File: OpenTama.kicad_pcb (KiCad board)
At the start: 2 copper layers, 45 x 58.2 mm, 65 parts, among them J1 Conn_01x09, J2 Conn_01x14, J3 Conn_01x07, J4 USB_C_Receptacle_USB2.0, J5 Conn_01x14, Q1 BSS138, Q2 BSS138, Q3 BSS84, SW1 LEFT, SW2 MIDDLE, SW3 RIGHT, U1 TPS62203DBV, U2 LTC4054ES5-4.2, U3 STM32L072CBTx, U4 USBLC6-2SC6, Y1 32768Hz - 12,5 pF

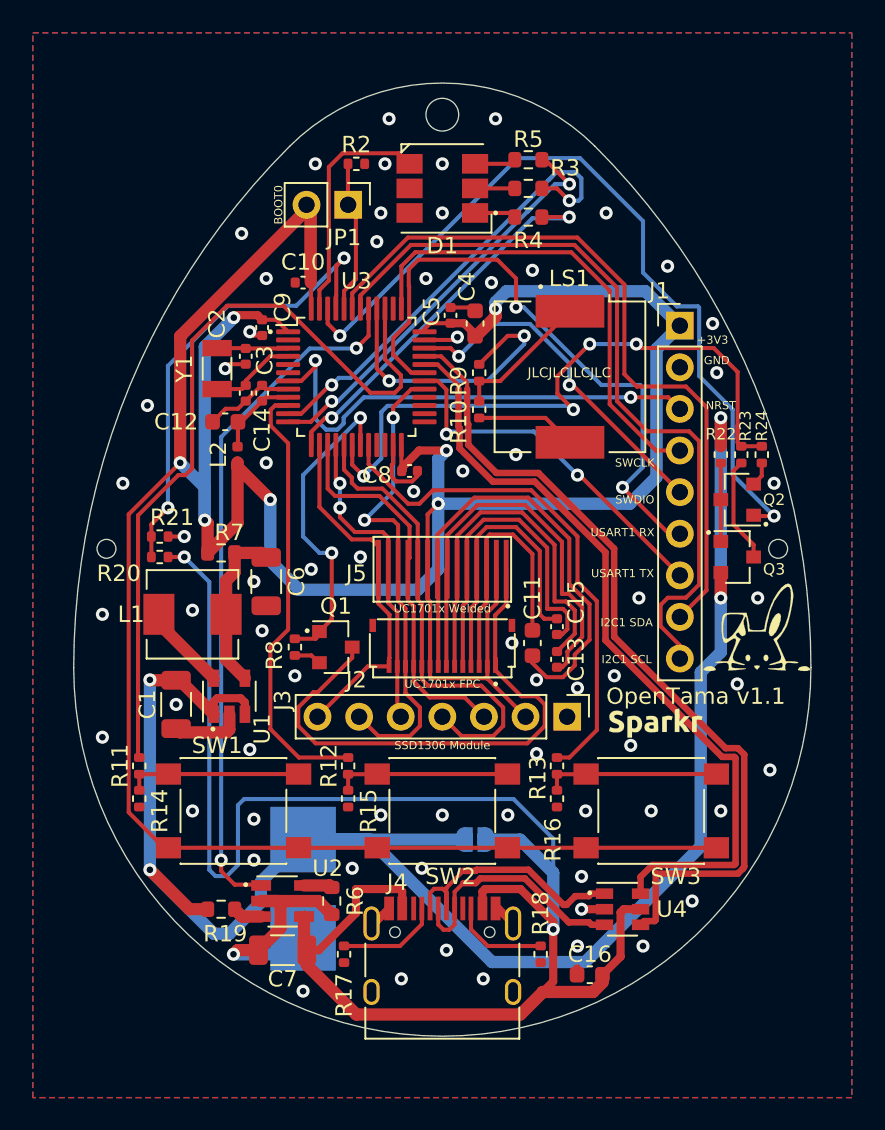
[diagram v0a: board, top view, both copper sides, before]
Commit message: Redesign with ESP32
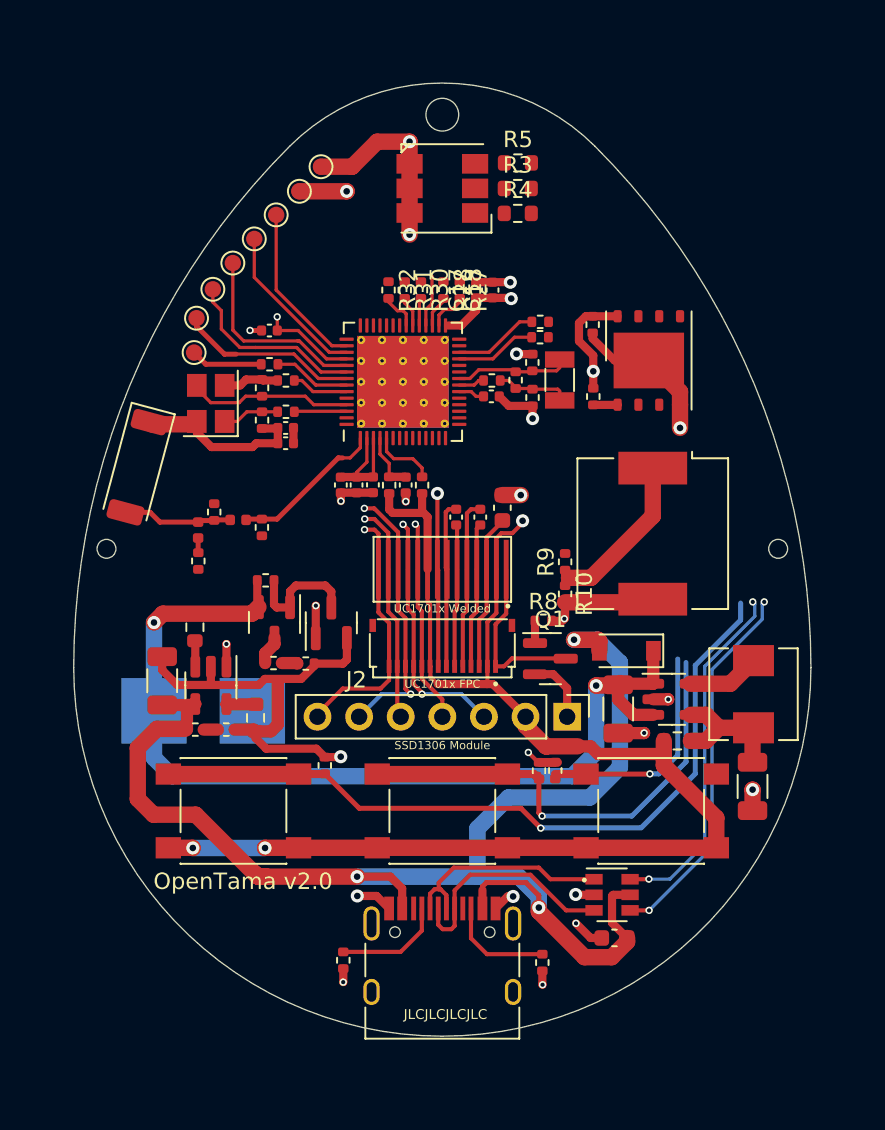
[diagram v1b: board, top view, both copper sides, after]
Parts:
- removed the G*** at (163.0, 104.5)
- removed J1: Conn_01x09, Connector_PinHeader_2.54mm:PinHeader_1x09_P2.54mm_Vertical
- removed JP1: BOOT0, Connector_PinHeader_2.54mm:PinHeader_1x02_P2.54mm_Vertical
- removed JP2: No BATT, Jumper:SolderJumper-2_P1.3mm_Open_RoundedPad1.0x1.5mm
- added AE1: Antenna_Chip, RF_Antenna:Johanson_2450AT43F0100, F.Cu at (131.4, 89.0)
- added C17: 1uF, Capacitor_SMD:C_0402_1005Metric, F.Cu at (152.1, 78.2)
- added C18: 0.1uF, Capacitor_SMD:C_0402_1005Metric, F.Cu at (153.1, 78.2)
- added C19: 10uF, Capacitor_SMD:C_0402_1005Metric, F.Cu at (143.8, 90.1)
- added C20: 0.1uF, Capacitor_SMD:C_0402_1005Metric, F.Cu at (139.4, 80.7)
- added C21: 1uF, Capacitor_SMD:C_0402_1005Metric, F.Cu at (140.4, 87.6)
- added C22: 1uF, Capacitor_SMD:C_0402_1005Metric, F.Cu at (144.8, 90.1)
- added C23: 0.1uF, Capacitor_SMD:C_0402_1005Metric, F.Cu at (140.4, 86.6)
- added C24: 0.1uF, Capacitor_SMD:C_0402_1005Metric, F.Cu at (145.8, 90.1)
- added C25: 0.1uF, Capacitor_SMD:C_0402_1005Metric, F.Cu at (153.0, 84.7)
- added D2: D_Small, Diode_SMD:D_SOD-123, F.Cu at (161.2, 100.2)
- added L3: L_Small, Inductor_SMD:L_0402_1005Metric, F.Cu at (137.5, 92.2)
- added R1: 10k, Resistor_SMD:R_0402_1005Metric, F.Cu at (155.9, 107.5)
- added R25: 10k, Resistor_SMD:R_0402_1005Metric, F.Cu at (146.8, 90.1)
- added R26: 499, Resistor_SMD:R_0402_1005Metric, F.Cu at (139.5, 82.7)
- added R27: 0R, Resistor_SMD:R_0402_1005Metric, F.Cu at (151.1, 78.2)
- added R28: 0R, Resistor_SMD:R_0402_1005Metric, F.Cu at (150.1, 78.2)
- added R30: 0R, Resistor_SMD:R_0402_1005Metric, F.Cu at (148.7, 78.2)
- added R31: 0R, Resistor_SMD:R_0402_1005Metric, F.Cu at (147.7, 78.2)
- added R32: 0R, Resistor_SMD:R_0402_1005Metric, F.Cu at (146.7, 78.2)
- added R33: 0R, Resistor_SMD:R_0402_1005Metric, F.Cu at (156.0, 81.1)
- added R34: 0R, Resistor_SMD:R_0402_1005Metric, F.Cu at (156.0, 80.1)
- added R35: 10k, Resistor_SMD:R_0402_1005Metric, F.Cu at (140.5, 83.7)
- added TP1: EN, TestPoint:TestPoint_Pad_D1.0mm, F.Cu at (141.3, 72.2)
- added TP2: TCK, TestPoint:TestPoint_Pad_D1.0mm, F.Cu at (139.9, 73.6)
- added TP3: MTMS, TestPoint:TestPoint_Pad_D1.0mm, F.Cu at (136.0, 78.2)
- added TP4: MTDO, TestPoint:TestPoint_Pad_D1.0mm, F.Cu at (138.5, 75.1)
- added TP5: MTDI, TestPoint:TestPoint_Pad_D1.0mm, F.Cu at (137.2, 76.6)
- added TP6: MTDI, TestPoint:TestPoint_Pad_D1.0mm, F.Cu at (142.6, 70.7)
- added TP7: RXD, TestPoint:TestPoint_Pad_D1.0mm, F.Cu at (134.8, 82.0)
- added TP8: TXD, TestPoint:TestPoint_Pad_D1.0mm, F.Cu at (135.0, 79.9)
- added U5: ESP32-S3R8V, Package_DFN_QFN:QFN-56-1EP_7x7mm_P0.4mm_EP5.6x5.6mm_ThermalVias, F.Cu at (147.6, 83.8)
- added Y2: 32k, Crystal:Crystal_SMD_3215-2Pin_3.2x1.5mm, F.Cu at (157.2, 83.7)
- C10, C5, C8, C9: value 100nF -> C_Small; footprint Capacitor_SMD:C_0402_1005Metric -> Resistor_SMD:R_0402_1005Metric
- C12: value 1uF -> C_Small; footprint Capacitor_SMD:C_0603_1608Metric -> Resistor_SMD:R_0402_1005Metric
- C14: value 10nF -> 1uF
- C2: value 12pF -> 0.1uF; footprint Capacitor_SMD:C_0402_1005Metric -> Resistor_SMD:R_0402_1005Metric
- C3: value 12pF -> C_Small; footprint Capacitor_SMD:C_0402_1005Metric -> Resistor_SMD:R_0402_1005Metric
- C4: value 10uF -> C_Small; footprint Capacitor_SMD:C_0603_1608Metric -> Resistor_SMD:R_0402_1005Metric
- G***: moved to B.Cu
- L2: value 39nH -> L_Small
- R11: value 330 -> 20k
- R12: value 330 -> 0R
- R13: value 330 -> 10k
- R14: value 220k -> 10k
- R15: value 220k -> 0R
- R16: value 220k -> DNP
- U3: value STM32L072CBTx -> W25Q32JVZP; footprint Package_QFP:LQFP-48_7x7mm_P0.5mm -> Package_SON:WSON-8-1EP_6x5mm_P1.27mm_EP3.4x4.3mm
- Y1: value 32768Hz - 12,5 pF -> 40mhz; footprint Crystal:Crystal_SMD_3215-2Pin_3.2x1.5mm -> Crystal:Crystal_SMD_3225-4Pin_3.2x2.5mm
- moved R2 39.0 mm to (156.9, 107.5), turned to 90 degrees
- moved L1 34.6 mm to (169.0, 102.9), turned to -90 degrees
- moved C6 32.2 mm to (168.9, 108.5)
- moved R23 31.3 mm to (139.7, 101.0), turned to 0 degrees
- moved R24 30.6 mm to (141.7, 101.0), turned to 0 degrees
- moved R7 30.1 mm to (164.3, 105.7)
- moved R22 28.8 mm to (139.2, 95.9), turned to 0 degrees
- moved Q3 28.5 mm to (139.8, 98.5), turned to -90 degrees
- moved U1 27.0 mm to (164.0, 103.2), turned to 0 degrees
- moved R15 27.0 mm to (153.0, 83.7), turned to 0 degrees
- moved C1 27.0 mm to (160.7, 103.8)
- moved Q2 25.9 mm to (143.2, 98.5), turned to 90 degrees
- moved R16 25.7 mm to (154.5, 83.7), turned to 90 degrees
- moved R11 24.3 mm to (148.8, 90.1)
- moved R13 22.7 mm to (159.2, 84.7), turned to -90 degrees
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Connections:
- C10 pad 1: +3V3 -> /ESP32-S3/MCU_XTAL32_N
- C12 pad 1: +3.3VA -> /ESP32-S3/LNA_IN
- C14 pad 1: +3.3VA -> /ESP32-S3/CHIP_PU
- C2 pad 1: OSC32_IN -> -BATT
- C2 pad 2: -BATT -> /ESP32-S3/VCC_SPI
- C3 pad 1: OSC32_OUT -> Net-(C3-Pad1)
- C4 pad 1: +3V3 -> -BATT
- C4 pad 2: -BATT -> /ESP32-S3/XTAL_P
- C5 pad 1: +3V3 -> -BATT
- C5 pad 2: -BATT -> /ESP32-S3/XTAL32_P
- C8 pad 1: +3V3 -> /ESP32-S3/RF_ANT
- C9 pad 1: +3V3 -> /ESP32-S3/MCU_XTAL_N
- J4 pad A8: Net-(J4-PadA8) -> unconnected-(J4-PadA8)
- J4 pad B8: Net-(J4-PadB8) -> unconnected-(J4-PadB8)
- J4 pad S1: -BATT -> unconnected-(J4-PadS1)
- L2 pad 1: +3V3 -> Net-(C3-Pad1)
- L2 pad 2: +3.3VA -> /ESP32-S3/RF_ANT
- R11 pad 1: Net-(R11-Pad1) -> +3V3
- R11 pad 2: LEFT_BTN -> /GPIO0
- R12 pad 1: Net-(R12-Pad1) -> /ESP32-S3/MCU_XTAL_P
- R12 pad 2: MIDDLE_BTN -> /ESP32-S3/XTAL_P
- R13 pad 1: Net-(R13-Pad1) -> /ESP32-S3/VCC_SPI
- R13 pad 2: RIGHT_BTN -> /ESP32-S3/MCU_SPICS0
- R14 pad 1: Net-(R11-Pad1) -> LEFT_BTN
- R15 pad 1: Net-(R12-Pad1) -> /ESP32-S3/MCU_XTAL32_P
- R15 pad 2: -BATT -> /ESP32-S3/XTAL32_P
- R16 pad 1: Net-(R13-Pad1) -> /ESP32-S3/XTAL32_P
- R16 pad 2: -BATT -> /ESP32-S3/MCU_XTAL32_N
- R2 pad 1: BOOT0 -> RIGHT_BTN
- SW1 pad 1: Net-(R11-Pad1) -> LEFT_BTN
- SW2 pad 1: Net-(R12-Pad1) -> MIDDLE_BTN
- SW3 pad 1: Net-(R13-Pad1) -> RIGHT_BTN
- U3 pad 1: +3V3 -> /ESP32-S3/MCU_SPICS0
- U3 pad 2: Net-(U3-Pad2) -> /ESP32-S3/SPIQ
- U3 pad 3: OSC32_IN -> /ESP32-S3/SPIWP
- U3 pad 4: OSC32_OUT -> -BATT
- U3 pad 5: Net-(U3-Pad5) -> /ESP32-S3/SPID
- U3 pad 6: Net-(U3-Pad6) -> /ESP32-S3/SPICLK
- U3 pad 7: NRST -> /ESP32-S3/SPIHD
- U3 pad 8: -BATT -> /ESP32-S3/VCC_SPI
- U3 pad 9: +3.3VA -> -BATT
- Y1 pad 1: OSC32_IN -> /ESP32-S3/XTAL_P
- Y1 pad 2: OSC32_OUT -> -BATT
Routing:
- net +3V3: track 217.2 -> 89.1 mm, vias 7 -> 4
- net +BATT: track 108.7 -> 58.0 mm, vias 4 -> 2
- net VBATT_MEAS: track 49.9 -> 1.98 mm, vias 2 -> 1
- net I2C1_SCL: track 47.2 -> 0.00 mm
- net I2C1_SDA: track 45.0 -> 0.00 mm
- net NCHARG: track 42.5 -> 1.39 mm, vias 2 -> 1
- net VBATT_ANA: track 40.2 -> 0.96 mm, vias 4 -> 0
- net USART1_RX: track 38.0 -> 0.00 mm, vias 2 -> 0
- net NRST: track 29.8 -> 0.00 mm, vias 2 -> 0
- net SWCLK: track 29.0 -> 0.00 mm
- net RED_LED: track 28.5 -> 0.00 mm, vias 2 -> 0
- net USB_D+: track 51.2 -> 22.9 mm, vias 0 -> 2
- net VBUS_SENSE: track 28.9 -> 0.87 mm, vias 2 -> 0
- net USB_D-: track 47.9 -> 21.6 mm, vias 0 -> 2
- net BLUE_LED: track 25.8 -> 0.00 mm, vias 2 -> 0
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- added copper zone on In1.Cu, net -BATT
- added copper zone on In2.Cu, net -BATT
- removed copper zone on B.Cu, net -BATT
- removed copper zone on F.Cu, net -BATT
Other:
- copper layers 2 -> 4
- net class Default removed
- net class USB removed
- board text added: "OpenTama v2.0"
- board text removed: "+3V3"
- board text removed: "+BATT"
- board text removed: "-BATT"
- board text removed: "BOOT0"
- board text removed: "Battery bypass (remove R19 as well)"
- board text removed: "GND"
- board text removed: "I2C1 SCL"
- board text removed: "I2C1 SDA"
- board text removed: "NRST"
- board text removed: "OpenTama v1.1"
- board text removed: "SWCLK"
- board text removed: "SWDIO"
- board text removed: "USART1 RX"
- board text removed: "USART1 TX"
